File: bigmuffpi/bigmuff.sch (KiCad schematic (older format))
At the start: 60 parts, among them J1 PWR JACK, J4 OUTPUT, J5 INPUT, Q1 BC239, Q2 BC239, Q3 BC239, Q4 BC239

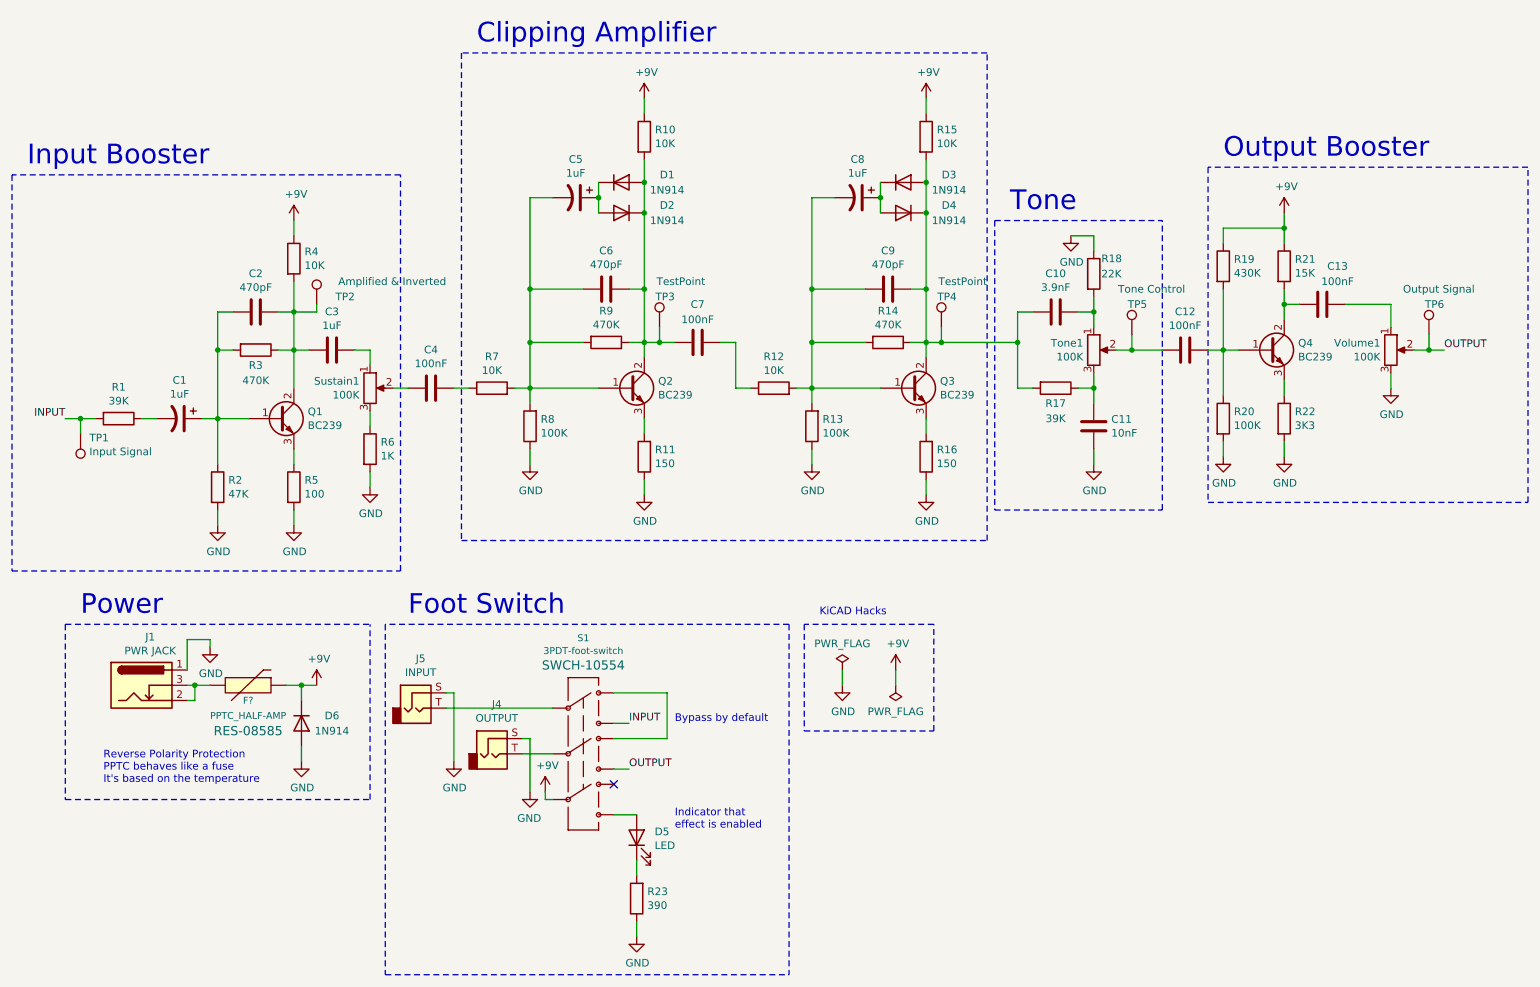
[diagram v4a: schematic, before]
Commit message: add: more testpoints
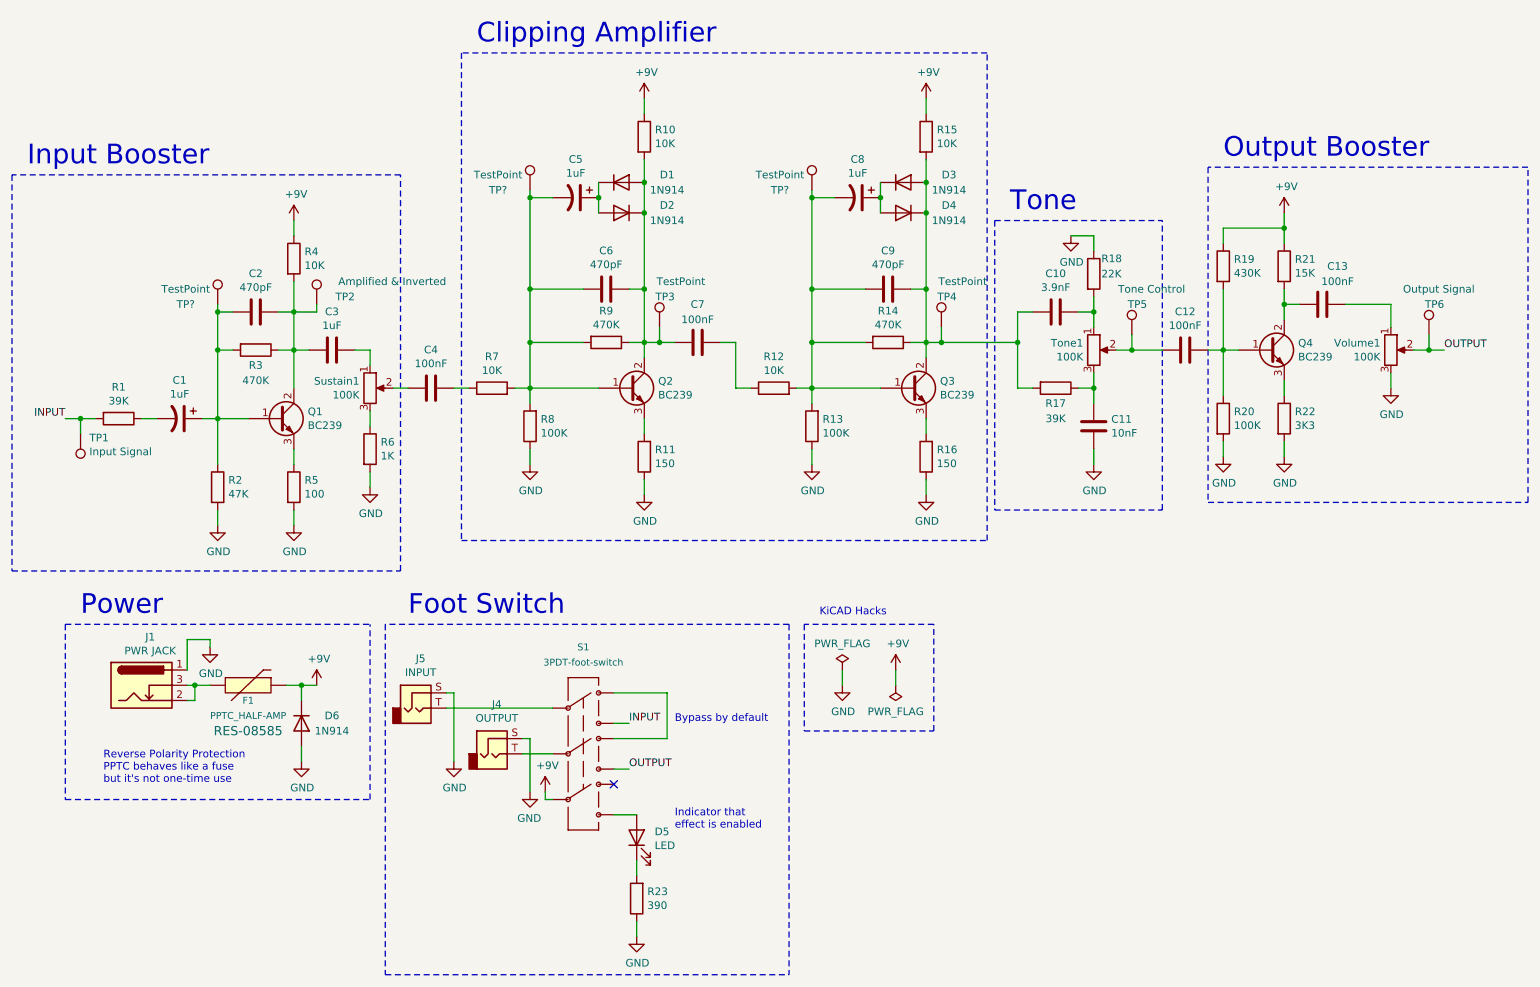
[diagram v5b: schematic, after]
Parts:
- added TP? (x3): TestPoint, TestPoint:TestPoint_Pad_2.0x2.0mm, symbol Connector:TestPoint
- gave numbers to parts that had none: 1
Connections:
- net at C1.1, C2.2, Q1.1 (B)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: now also TP?.1
- net at C5.2, C6.2, Q2.1 (B)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: now also TP?.1
- net at C8.2, C9.2, Q3.1 (B)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: now also TP?.1
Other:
- note added: "Reverse Polarity Protection\nPPTC behaves like a fuse\nbut it's not one-time use"
- note removed: "Reverse Polarity Protection\nPPTC behaves like a fuse\nIt's based on the temperature"
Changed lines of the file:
@@
 U 1 1 5F097466
 P 4850 6000
-F 0 "S1" H 4850 6560 45  0000 C CNN
-F 1 "3PDT-foot-switch" H 4850 6476 45  0000 C CNN
+F 0 "S1" H 4850 6500 45  0000 C CNN
+F 1 "3PDT-foot-switch" H 4850 6400 45  0000 C CNN
 F 2 "bigmuffpi:SF17020F-0302-21R-L" H 4850 6450 20  0001 C CNN
 F 3 "https://cz.mouser.com/datasheet/2/13/SF17_SF12030F-1155740.pdf" H 4850 6000 50  0001 C CNN
-F 4 "SWCH-10554" H 4850 6381 60  0000 C CNN "Field4"
+F 4 "SWCH-10554" H 4850 6381 60  0001 C CNN "Field4"
 F 5 "3PDT 9-Pin" H 4850 6000 50  0001 C CNN "Mfr. No"
 F 6 "107-SF17020F-32-21RL" H 4850 6000 50  0001 C CNN "Mouser"
@@
 	2250 5650 2250 5450
 $Comp
-L SparkFun-Fuses:PPTC_HALF-AMP F?
+L SparkFun-Fuses:PPTC_HALF-AMP F1
 U 1 1 5F449675
 P 2600 5750
-F 0 "F?" H 2650 5650 45  0000 C CNN
+F 0 "F1" H 2650 5650 45  0000 C CNN
 F 1 "PPTC_HALF-AMP" H 2650 5550 45  0000 C CNN
 F 2 "1206" H 2600 5950 20  0001 C CNN
@@
 $EndComp
 $Comp
-L power:GND #PWR?
+L power:GND #PWR020
 U 1 1 5F44D824
 P 3000 6250
-F 0 "#PWR?" H 3000 6000 50  0001 C CNN
+F 0 "#PWR020" H 3000 6000 50  0001 C CNN
 F 1 "GND" H 3005 6077 50  0000 C CNN
 F 2 "" H 3000 6250 50  0001 C CNN
@@
 	2400 5450 2400 5500
 Text Notes 1700 6400 0    50   ~ 0
-Reverse Polarity Protection\nPPTC behaves like a fuse\nIt's based on the temperature
+Reverse Polarity Protection\nPPTC behaves like a fuse\nbut it's not one-time use
 Wire Notes Line
 	1450 5350 1450 6500
@@
 Wire Notes Line
 	1450 5350 3450 5350
+$Comp
+L Connector:TestPoint TP?
+U 1 1 5F5852AE
+P 2450 3250
+F 0 "TP?" H 2300 3250 50  0000 R CNN
+F 1 "TestPoint" H 2400 3350 50  0000 R CNN
+F 2 "TestPoint:TestPoint_Pad_2.0x2.0mm" H 2650 3250 50  0001 C CNN
+F 3 "~" H 2650 3250 50  0001 C CNN
+F 4 "~" H 2450 3250 50  0001 C CNN "Supplier"
+	1    2450 3250
+	1    0    0    -1
+$EndComp
+Wire Wire Line
+	2450 3250 2450 3300
+Connection ~ 2450 3300
+$Comp
+L Connector:TestPoint TP?
+U 1 1 5F59ACBE
+P 4500 2500
+F 0 "TP?" H 4350 2500 50  0000 R CNN
+F 1 "TestPoint" H 4450 2600 50  0000 R CNN
+F 2 "TestPoint:TestPoint_Pad_2.0x2.0mm" H 4700 2500 50  0001 C CNN
+F 3 "~" H 4700 2500 50  0001 C CNN
+F 4 "~" H 4500 2500 50  0001 C CNN "Supplier"
+	1    4500 2500
+	1    0    0    -1
+$EndComp
+Wire Wire Line
+	4500 2500 4500 2550
+Connection ~ 4500 2550
+$Comp
+L Connector:TestPoint TP?
+U 1 1 5F5A9929
+P 6350 2500
+F 0 "TP?" H 6200 2500 50  0000 R CNN
+F 1 "TestPoint" H 6300 2600 50  0000 R CNN
+F 2 "TestPoint:TestPoint_Pad_2.0x2.0mm" H 6550 2500 50  0001 C CNN
+F 3 "~" H 6550 2500 50  0001 C CNN
+F 4 "~" H 6350 2500 50  0001 C CNN "Supplier"
+	1    6350 2500
+	1    0    0    -1
+$EndComp
+Wire Wire Line
+	6350 2500 6350 2550
+Connection ~ 6350 2550
 $EndSCHEMATC
